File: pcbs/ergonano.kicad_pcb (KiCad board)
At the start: 2 copper layers, 167.6 x 164.6 mm, 94 parts

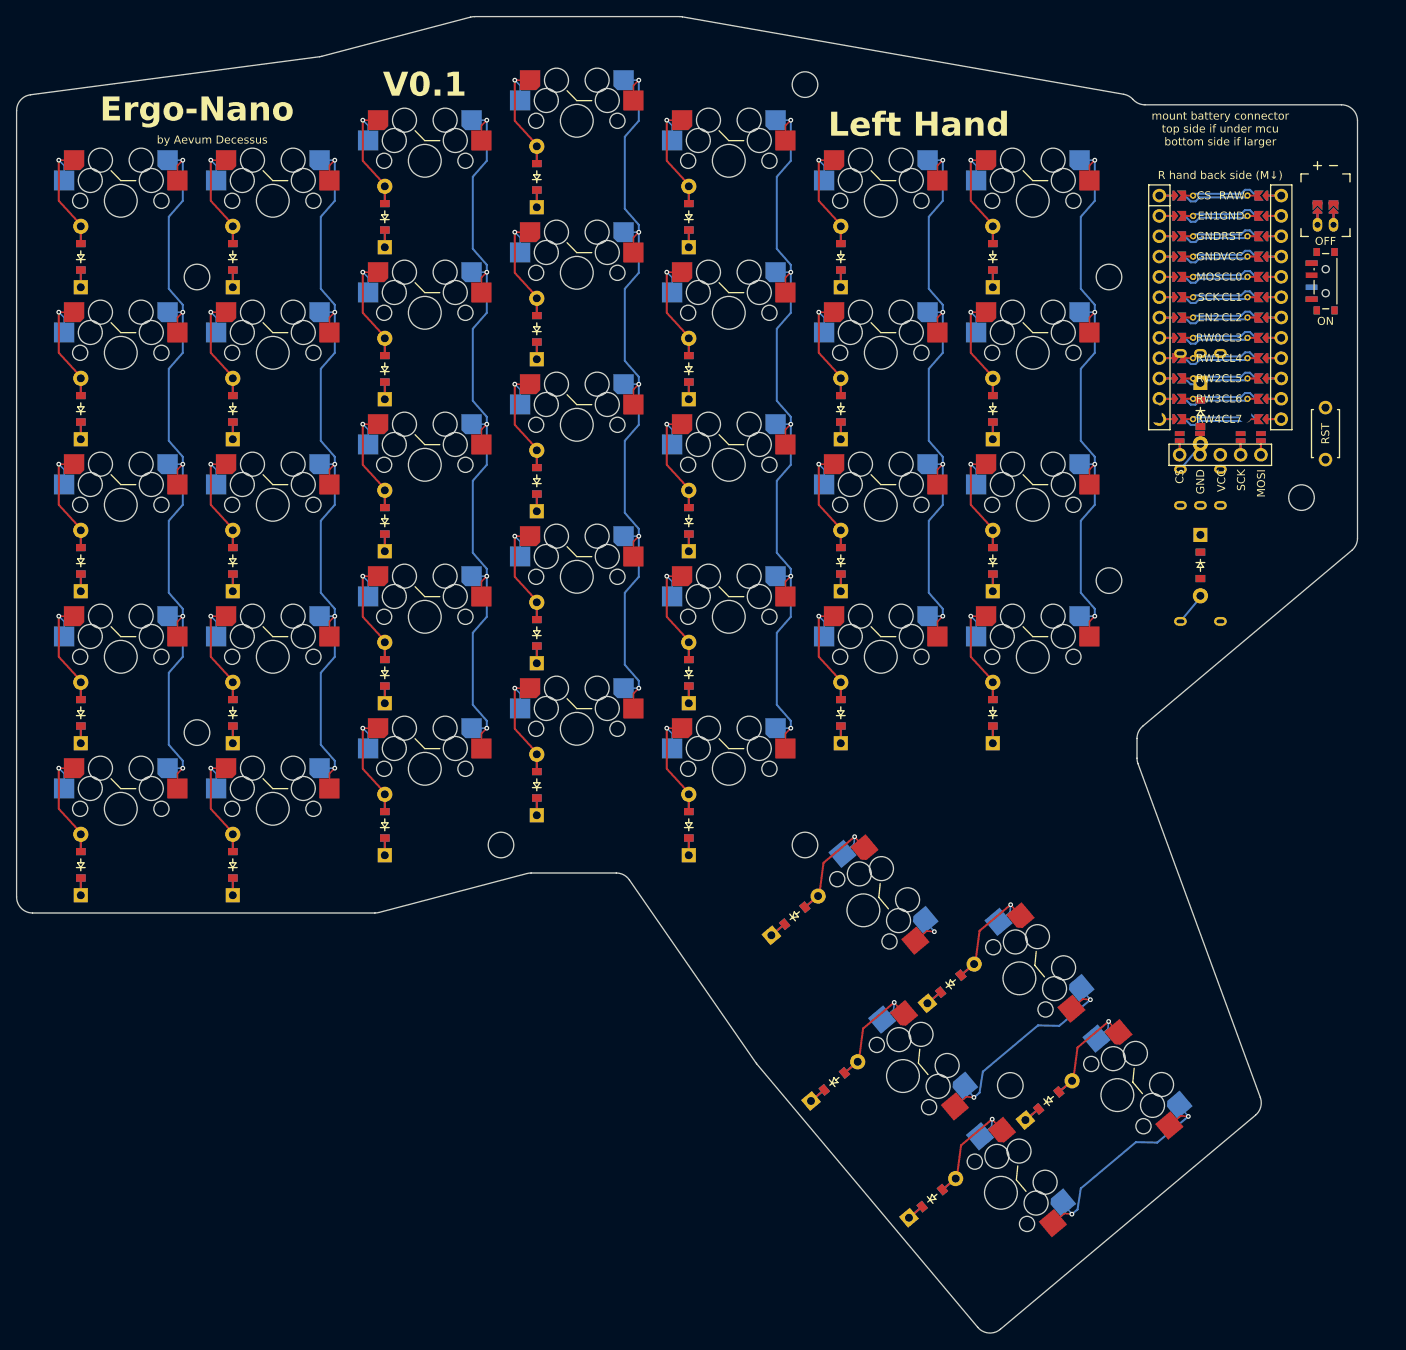
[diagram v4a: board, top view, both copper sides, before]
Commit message: Removed accidental 2nd encoder, added more data to key switches
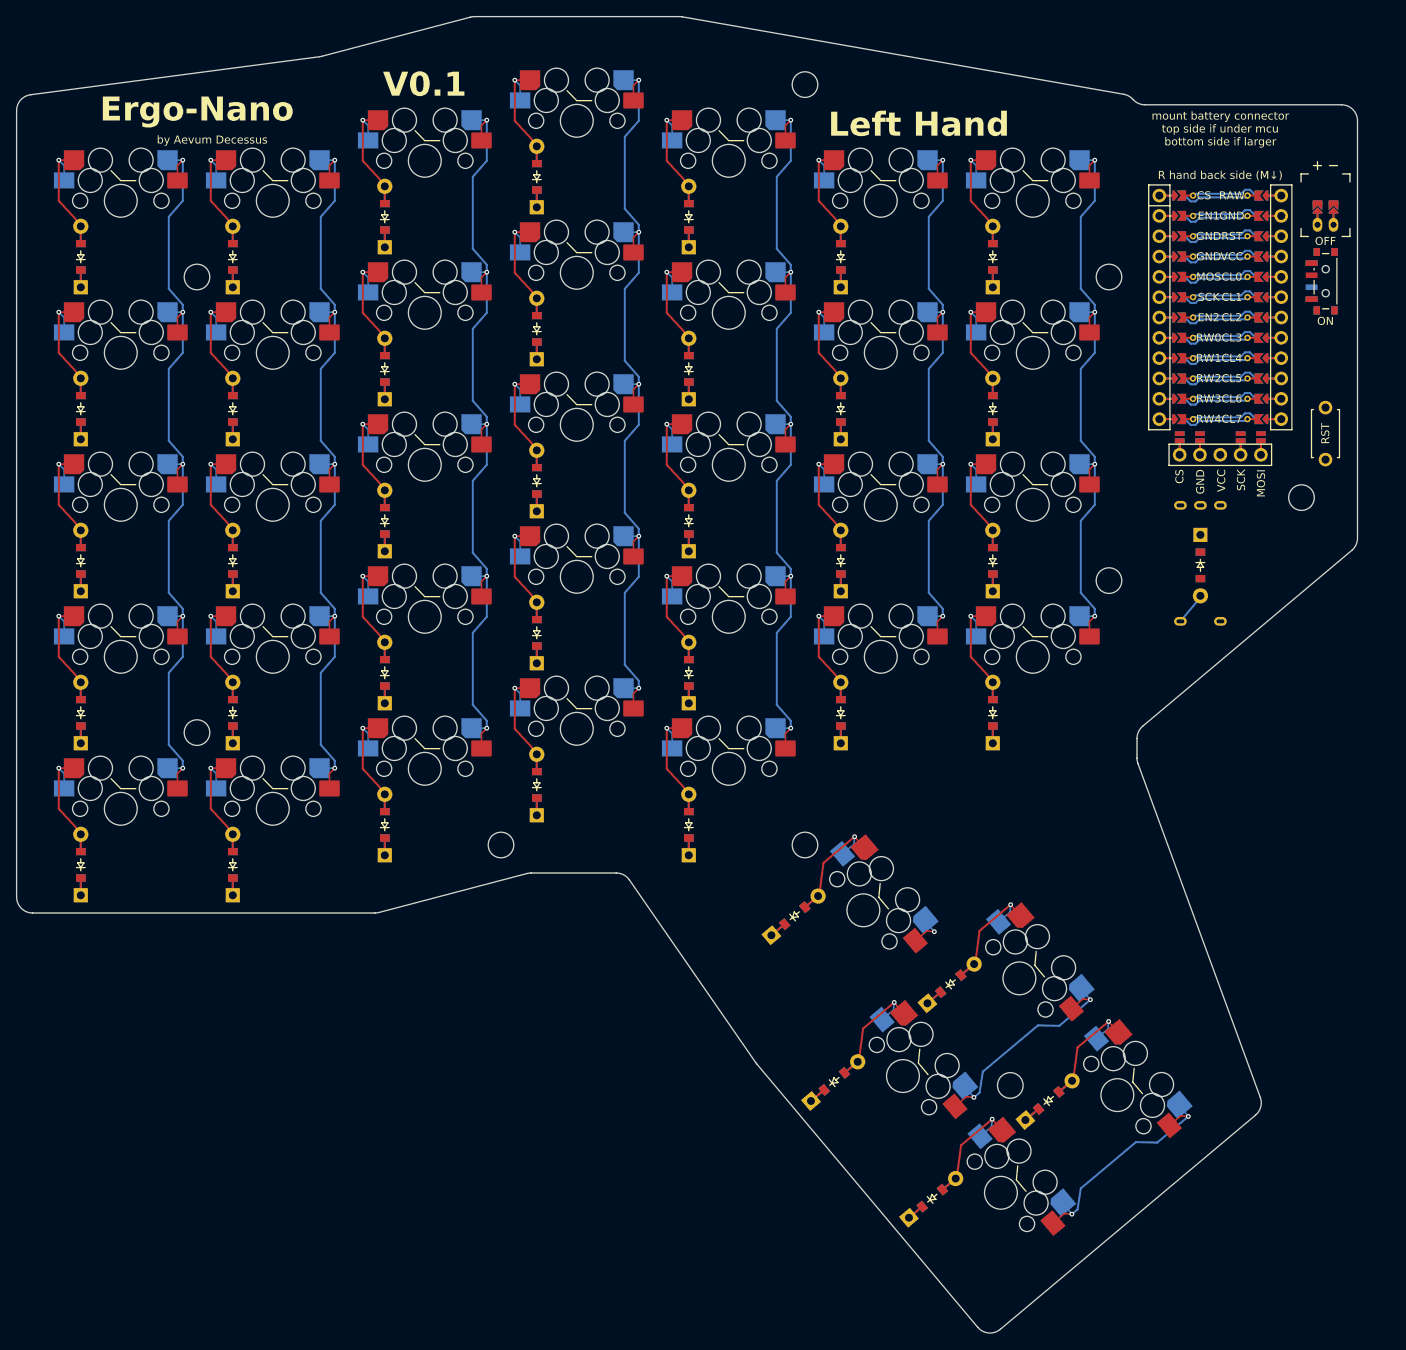
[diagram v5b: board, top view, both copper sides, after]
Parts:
- removed D40: , ceoloide:diode_tht_sod123
- removed RE2: , ceoloide:rotary_encoder_ec11_ec12
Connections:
- D39 pad 1: (no net) -> RW4
- D39 pad 2: encoder_mcu -> encoder_encoder
- RE1 pad S2: encoder_mcu -> encoder_encoder
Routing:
- net (no net): track 922.0 -> 918.1 mm

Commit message: make net names shorter, build tweaks
be more granular with JLCPCB requirements
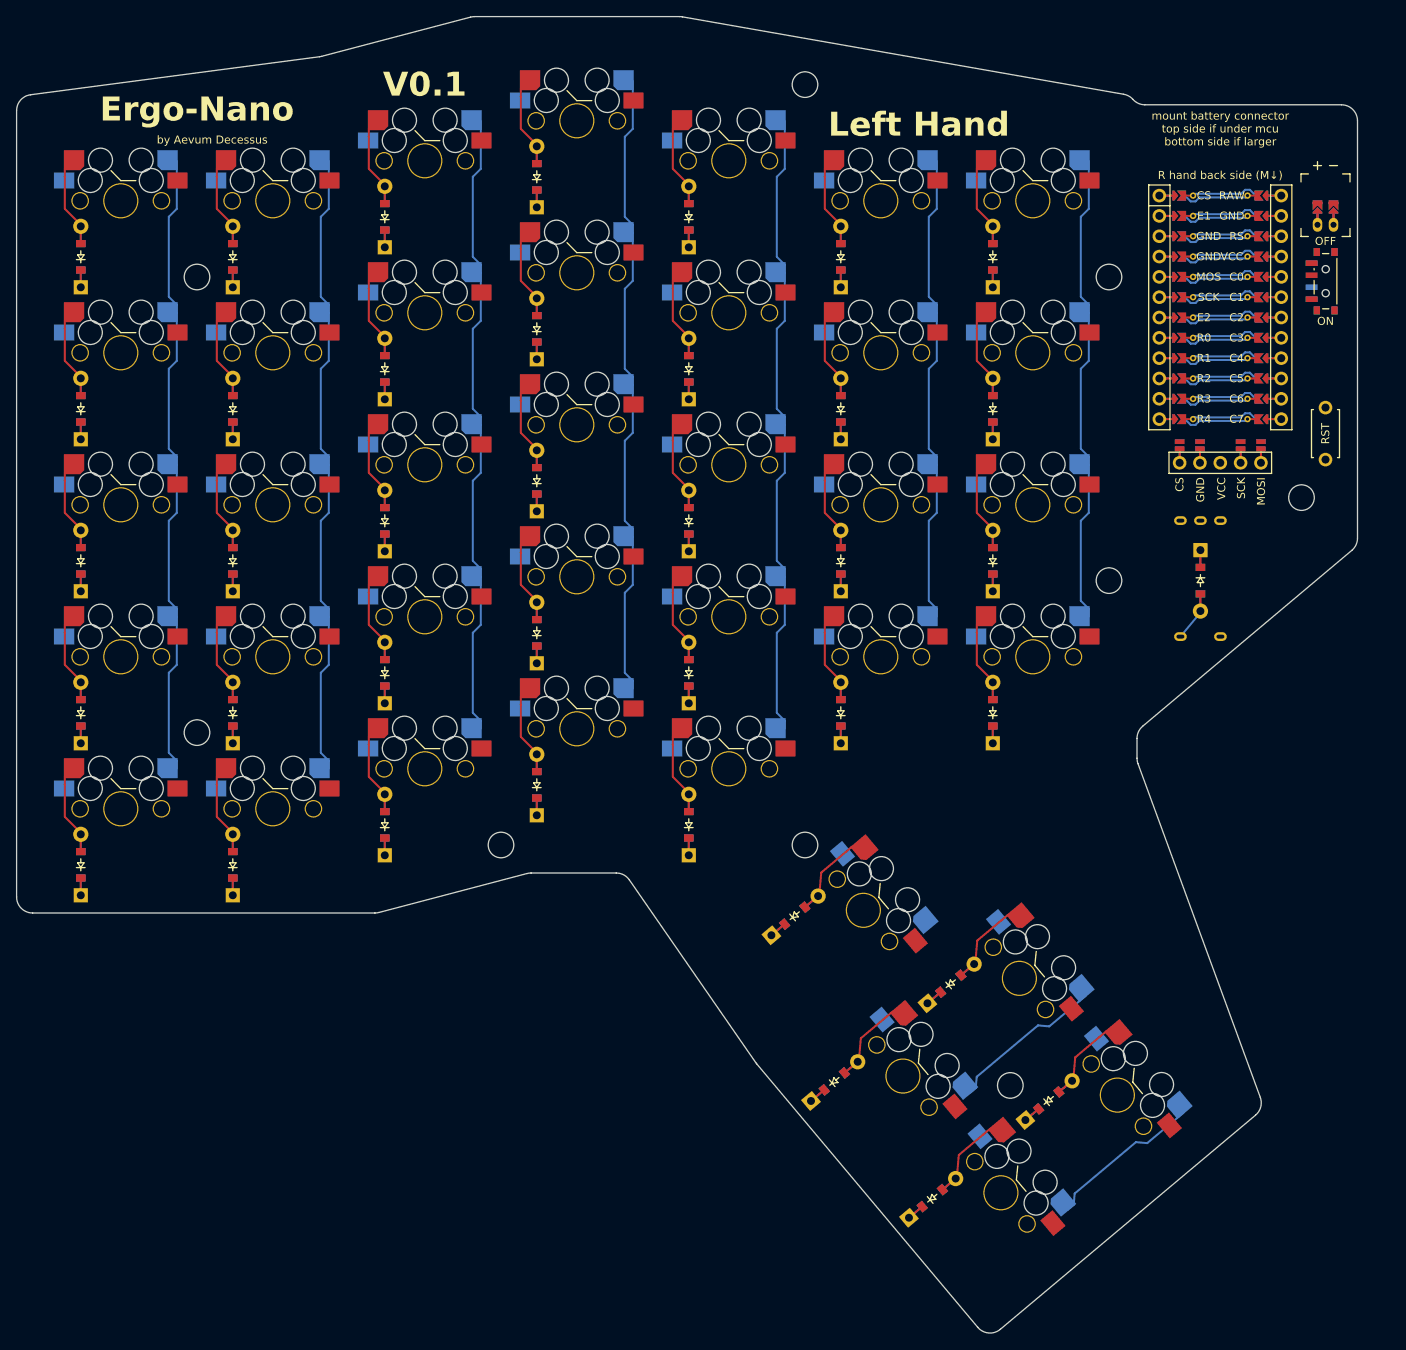
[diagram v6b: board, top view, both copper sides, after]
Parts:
- moved D39 1.91 mm to (185.0, 96.5)
- moved RE1 1.91 mm to (185.0, 96.5)
- moved DISP1 1.00 mm to (187.4, 65.0)
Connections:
- net CL0 renamed C0
- net CL1 renamed C1
- net CL2 renamed C2
- net CL3 renamed C3
- net CL4 renamed C4
- net CL5 renamed C5
- net CL6 renamed C6
- net CL7 renamed C7
- net EN1 renamed E1
- net EN2 renamed E2
- net RST renamed RS
- net RW0 renamed R0
- net RW1 renamed R1
- net RW2 renamed R2
- net RW3 renamed R3
- net RW4 renamed R4
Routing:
- net C3: track 23.6 -> 0.00 mm, vias 5 -> 0
- net C2: track 23.6 -> 0.00 mm, vias 5 -> 0
- net C1: track 23.6 -> 0.00 mm, vias 5 -> 0
- net C0: track 23.6 -> 0.00 mm, vias 5 -> 0
- net C4: track 23.6 -> 0.00 mm, vias 5 -> 0
- net C7: track 23.6 -> 0.00 mm, vias 5 -> 0
- net C6: track 18.9 -> 0.00 mm, vias 4 -> 0
- net C5: track 18.9 -> 0.00 mm, vias 4 -> 0
- net (no net): track 918.1 -> 904.5 mm
- net t_col2_near: track 18.1 -> 12.1 mm, vias 1 -> 0
- net t_col2_far: track 18.1 -> 12.1 mm, vias 1 -> 0
- net t_col1_near: track 18.1 -> 12.1 mm, vias 1 -> 0
- net t_col1_far: track 18.1 -> 12.1 mm, vias 1 -> 0
- net t_col0_near: track 18.1 -> 12.1 mm, vias 1 -> 0
- net ring_top: track 18.1 -> 12.1 mm, vias 1 -> 0
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
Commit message: Added silkscreen labels for switch rows, nets, and names
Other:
- board text added: "C0"
- board text added: "C1"
- board text added: "C2"
- board text added: "C3"
- board text added: "C4"
- board text added: "C5"
- board text added: "C6"
- board text added: "C7"
- board text added: "R0"
- board text added: "R1"
- board text added: "R2"
- board text added: "R3"
- board text added: "R4"
- board text added: "index_bottom"
- board text added: "index_home"
- board text added: "index_mod"
- board text added: "index_num"
- board text added: "index_top"
- board text added: "inner_bottom"
- board text added: "inner_home"
- board text added: "inner_num"
- board text added: "inner_top"
- board text added: "innermod_bottom"
- board text added: "innermod_home"
- board text added: "innermod_num"
- board text added: "innermod_top"
- board text added: "middle_bottom"
- board text added: "middle_home"
- board text added: "middle_mod"
- board text added: "middle_num"
- board text added: "middle_top"
- board text added: "outer_bottom"
- board text added: "outer_home"
- board text added: "outer_mod"
- board text added: "outer_num"
- board text added: "outer_top"
- board text added: "pinky_bottom"
- board text added: "pinky_home"
- board text added: "pinky_mod"
- board text added: "pinky_num"
- board text added: "pinky_top"
- board text added: "ring_bottom"
- board text added: "ring_home"
- board text added: "ring_mod"
- board text added: "ring_num"
- board text added: "ring_top"
- board text added: "t_col0_near"
- board text added: "t_col1_far"
- board text added: "t_col1_near"
- board text added: "t_col2_far"
- board text added: "t_col2_near"
